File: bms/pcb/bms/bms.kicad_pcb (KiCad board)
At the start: 2 copper layers, 52.7 x 86.2 mm, 40 parts, among them IC1 NCV8402ASTT1G, IC2 NCV8402ASTT1G, IC3 MCP2515-I_ST, IC4 MCP2515-I_ST, IC5 MCP2515-I_ST, IC6 SN65HVD230, IC7 SN65HVD230, IC8 SN65HVD230, IC9 TPS62160DGKR, J1 power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

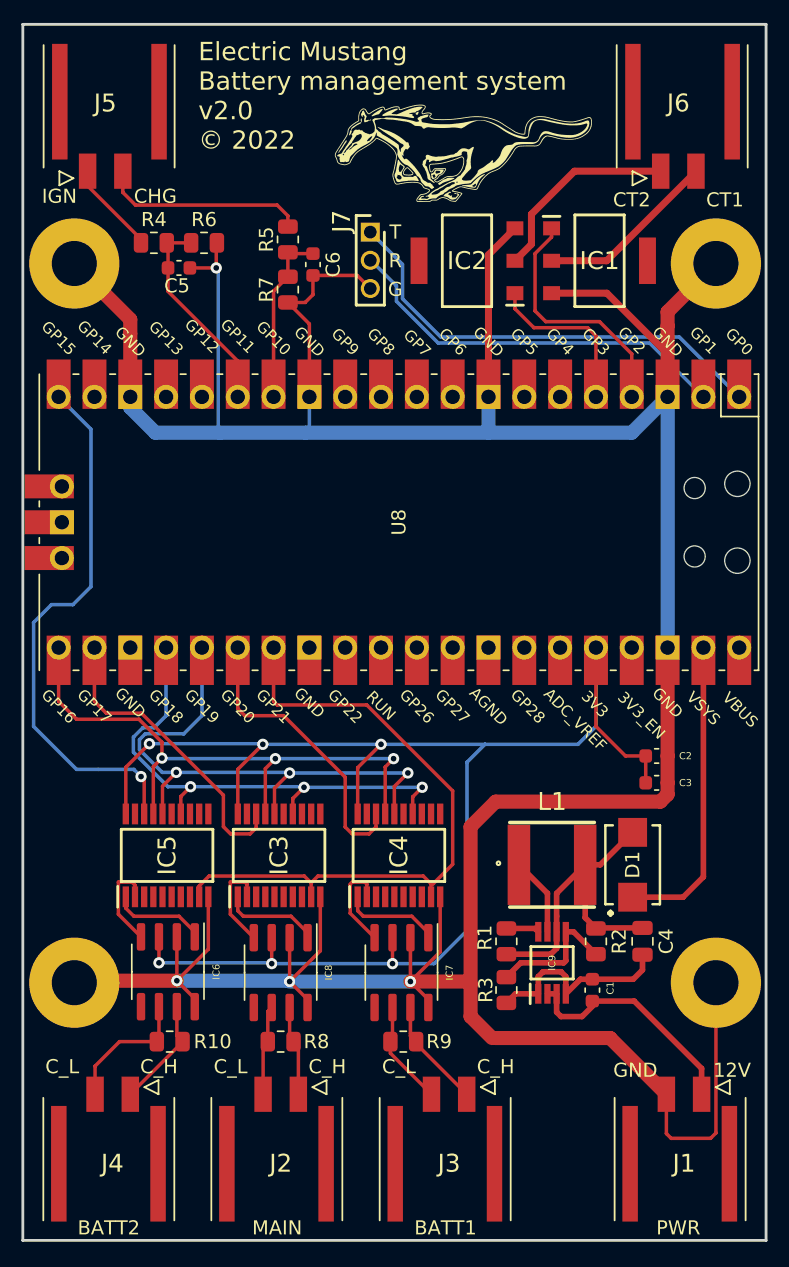
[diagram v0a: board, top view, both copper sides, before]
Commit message: Found two more errors in bms. Create version 3
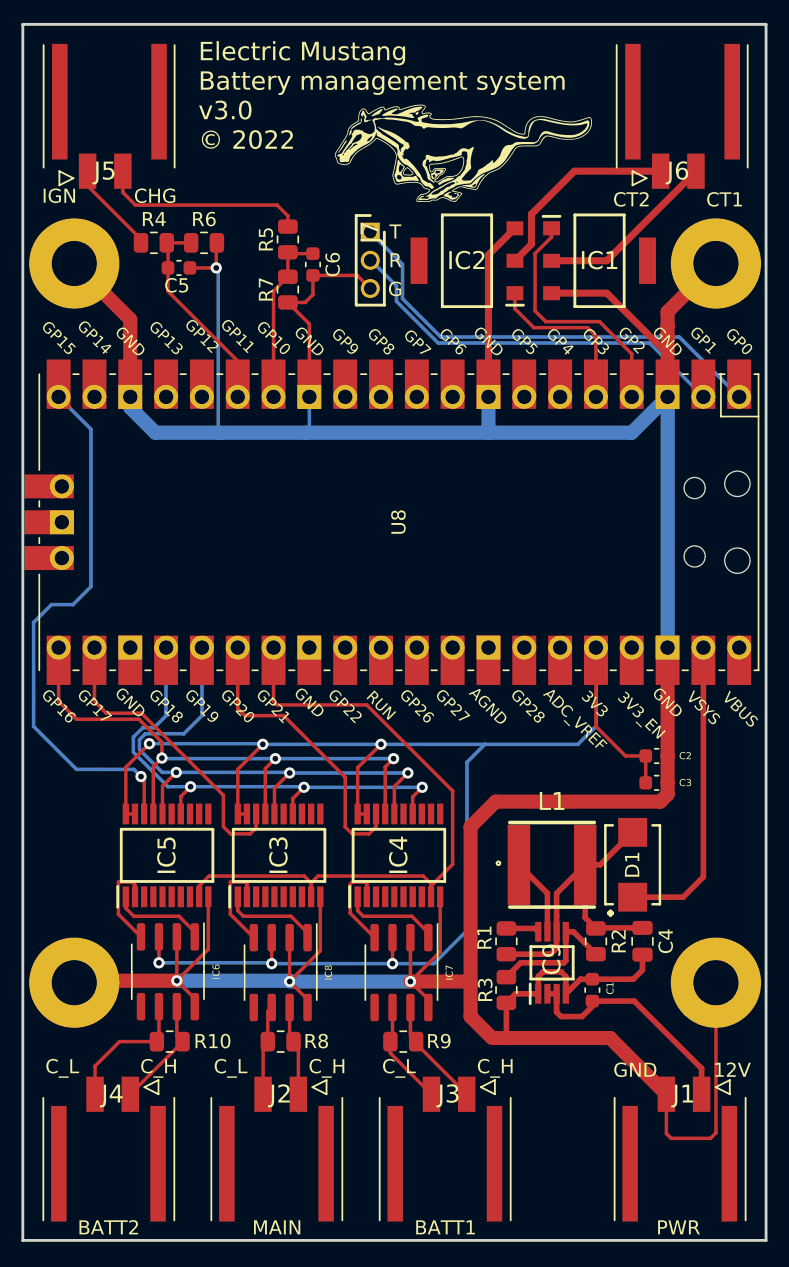
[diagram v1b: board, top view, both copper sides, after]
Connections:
- C1 pad 2: Net-(C1-Pad2) -> GND
- C4 pad 2: Net-(C1-Pad2) -> GND
- IC3 pad 19: unconnected-(IC3-Pad19) -> 3V
- IC4 pad 19: unconnected-(IC4-Pad19) -> 3V
- IC5 pad 19: unconnected-(IC5-Pad19) -> 3V
- IC9 pad 1: Net-(C1-Pad2) -> GND
- IC9 pad 4: Net-(C1-Pad2) -> GND
- R3 pad 2: Net-(C1-Pad2) -> GND
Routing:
- net GND: track 279.6 -> 296.5 mm
- net Net-(C1-Pad2): track 14.4 -> 0.00 mm
- net 3V: track 108.7 -> 110.7 mm
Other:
- board text added: "Electric Mustang Battery management system v3.0 © 2022"
- board text removed: "Electric Mustang Battery management system v2.0 © 2022"

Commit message: BMS pcb v4
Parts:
- removed H1, H2, H3, H4: MountingHole, MountingHole:MountingHole_3.2mm_M3_Pad
- removed J1: power, Connector:105430YY02
- removed J2: MAIN CAN, Connector:105430YY02
- removed J3: BATT1 CAN, Connector:105430YY02
- removed J4: BATT2 CAN, Connector:105430YY02
- removed J5, J6: INPUTS, Connector:105430YY02
- added C10: 1uF, Capacitor_SMD:C_0603_1608Metric, F.Cu at (121.6, 111.4)
- added C7: 1uF, Capacitor_SMD:C_0603_1608Metric, F.Cu at (121.6, 100.7)
- added C8: 1uF, Capacitor_SMD:C_0603_1608Metric, F.Cu at (121.6, 104.2)
- added C9: 1uF, Capacitor_SMD:C_0603_1608Metric, F.Cu at (121.6, 107.6)
- added IC10: NCV8402ASTT1G, Symbol:SOT230P700X175-4N, F.Cu at (105.3, 72.5)
- added IC11: NCV8402ASTT1G, Symbol:SOT230P700X175-4N, F.Cu at (113.7, 72.5)
- added IC12: NCV8402ASTT1G, Symbol:SOT230P700X175-4N, F.Cu at (105.3, 83.7)
- added IC13: NCV8402ASTT1G, Symbol:SOT230P700X175-4N, F.Cu at (113.7, 83.7)
- added JP1: SolderJumper_2_Open, Jumper:SolderJumper-2_P1.3mm_Open_Pad1.0x1.5mm, F.Cu at (145.7, 136.7)
- added JP2: SolderJumper_2_Open, Jumper:SolderJumper-2_P1.3mm_Open_Pad1.0x1.5mm, F.Cu at (136.6, 136.7)
- added JP3: SolderJumper_2_Open, Jumper:SolderJumper-2_P1.3mm_Open_Pad1.0x1.5mm, F.Cu at (127.7, 136.7)
- added R11: 4k7, Resistor_SMD:R_0805_2012Metric, F.Cu at (114.2, 100.0)
- added R12: 4k7, Resistor_SMD:R_0805_2012Metric, F.Cu at (114.2, 105.0)
- added R13: 4k7, Resistor_SMD:R_0805_2012Metric, F.Cu at (114.2, 107.1)
- added R14: 4k7, Resistor_SMD:R_0805_2012Metric, F.Cu at (114.2, 112.0)
- added R15: 1k5, Resistor_SMD:R_0805_2012Metric, F.Cu at (117.8, 100.7)
- added R16: 1k5, Resistor_SMD:R_0805_2012Metric, F.Cu at (117.8, 104.2)
- added R17: 1k5, Resistor_SMD:R_0805_2012Metric, F.Cu at (117.8, 107.8)
- added R18: 1k5, Resistor_SMD:R_0805_2012Metric, F.Cu at (117.8, 111.4)
- added X1: ATM13-12PB-12PC-BM03, Connector:ATM1312PB12PCBM03, F.Cu at (118.3, 146.0)
- J7: footprint Connector:HDRV3W50P0X200_1X3_600X200X525P -> Connector_PinHeader_2.54mm:PinHeader_1x03_P2.54mm_Vertical
- moved U8 66.7 mm to (153.7, 83.1), turned to 0 degrees
- moved R3 63.1 mm to (165.2, 134.5)
- moved IC3 59.6 mm to (143.9, 120.4)
- moved IC8 59.2 mm to (143.9, 129.5)
- moved R2 58.2 mm to (166.5, 131.0), turned to 180 degrees
- moved J7 57.0 mm to (137.2, 58.9), turned to 0 degrees
- moved D1 56.8 mm to (167.5, 125.1), turned to -90 degrees
- moved R8 56.8 mm to (142.2, 136.7)
- moved L1 56.2 mm to (161.1, 125.1)
- moved IC9 56.0 mm to (161.2, 133.0)
- moved R1 55.6 mm to (157.3, 130.7), turned to -90 degrees
- moved C4 55.1 mm to (167.5, 134.5)
- moved IC5 50.5 mm to (126.2, 120.4)
- moved IC6 50.1 mm to (126.2, 129.5)
- moved C1 50.0 mm to (157.6, 134.3)
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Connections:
- net BATT_1_CONTACTOR_SIGNAL renamed BATT_1_INHIBIT_SIGNAL
- net BATT_2_CONTACTOR_SIGNAL renamed BATT_2_INHIBIT_SIGNAL
- IC1 pad 2: BATT_1_CONTACTOR_GND -> BATT_1_INHIBIT
- IC2 pad 2: BATT_2_CONTACTOR_GND -> BATT_2_INHIBIT
- R10 pad 2: BATT_2_CAN_H -> Net-(JP3-Pad1)
- R8 pad 2: MAIN_CAN_H -> Net-(JP1-Pad1)
- R9 pad 2: BATT_1_CAN_H -> Net-(JP2-Pad1)
- U8 pad 10: unconnected-(U8-Pad10) -> OUT_4_SIGNAL
- U8 pad 12: unconnected-(U8-Pad12) -> CHARGE_ENABLE_IN_SIGNAL
- U8 pad 14: CHARGE_ENABLE_IN_SIGNAL -> IGNITION_ON_IN_SIGNAL
- U8 pad 15: IGNITION_ON_IN_SIGNAL -> IN_1_SIGNAL
- U8 pad 16: unconnected-(U8-Pad16) -> IN_2_SIGNAL
- U8 pad 17: unconnected-(U8-Pad17) -> IN_3_SIGNAL
- U8 pad 19: unconnected-(U8-Pad19) -> IN_4_SIGNAL
- U8 pad 23: unconnected-(U8-Pad23) -> GND
- U8 pad 28: unconnected-(U8-Pad28) -> GND
- U8 pad 33: unconnected-(U8-Pad33) -> GND
- U8 pad 6: unconnected-(U8-Pad6) -> OUT_1_SIGNAL
- U8 pad 7: unconnected-(U8-Pad7) -> OUT_2_SIGNAL
- U8 pad 9: unconnected-(U8-Pad9) -> OUT_3_SIGNAL
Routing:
- net GND: track 296.5 -> 726.4 mm, vias 4 -> 12
- net BATT_2_INHIBIT: track 0.00 -> 110.5 mm
- net BATT_1_INHIBIT: track 0.00 -> 96.5 mm
- net OUT_2: track 0.00 -> 92.6 mm
- net OUT_1: track 0.00 -> 91.2 mm
- net OUT_3: track 0.00 -> 80.5 mm
- net OUT_4: track 0.00 -> 73.6 mm
- net IN_1: track 0.00 -> 57.1 mm
- net IN_3: track 0.00 -> 49.4 mm
- net CHARGE_ENABLE_IN: track 14.7 -> 63.9 mm
- net Net-(D1-Pad1): track 21.9 -> 70.7 mm
- net IGNITION_ON_IN: track 6.65 -> 51.9 mm
- net 3V: track 110.7 -> 155.8 mm, vias 6 -> 7
- net IN_2: track 0.00 -> 44.5 mm
- net 5V: track 23.0 -> 65.8 mm
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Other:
- board size 52.7 x 86.2 mm -> 82.6 x 100.6 mm
- board text added: "COMMS"
- board text added: "DIGITAL IN"
- board text added: "Electric Mustang Battery management system v4.0 © 2022"
- board text added: "LOW SIDE SWITCHES"
- board text added: "POWER"
- board text added: "RX"
- board text added: "TX"
- board text removed: "12V"
- board text removed: "BATT1"
- board text removed: "BATT2"
- board text removed: "CHG"
- board text removed: "CT1"
- board text removed: "CT2"
- board text removed: "C_H"
- board text removed: "C_L"
- board text removed: "Electric Mustang Battery management system v3.0 © 2022"
- board text removed: "G"
- board text removed: "IGN"
- board text removed: "MAIN"
- board text removed: "PWR"
- board text removed: "R"
- board text removed: "T"
